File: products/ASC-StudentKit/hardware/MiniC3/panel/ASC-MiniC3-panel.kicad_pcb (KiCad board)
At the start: 2 copper layers, 96 x 100 mm, 128 parts, among them J1_1 PUMP, J1_2 PUMP, J1_3 PUMP, J1_4 PUMP, J1_5 CABLE, J1_6 CABLE, J1_7 CABLE, J1_8 CABLE, J3_1 AUX, J3_2 AUX, J3_3 AUX, J3_4 AUX, J4_1 FLOW (XH or 3.5 mm), J4_2 FLOW (XH or 3.5 mm), J4_3 FLOW (XH or 3.5 mm), J4_4 FLOW (XH or 3.5 mm), J5_1 I2C, J5_2 I2C, J5_3 I2C, J5_4 I2C, J6_1 RELAY 230V (MSTBVA), J6_2 RELAY 230V (MSTBVA), J6_3 RELAY 230V (MSTBVA), J6_4 RELAY 230V (MSTBVA), K1_1 HF46F/005-HS1, K1_2 HF46F/005-HS1, K1_3 HF46F/005-HS1, K1_4 HF46F/005-HS1, U1_1 ESP32-C3 Super Mini, U1_2 ESP32-C3 Super Mini, U1_3 ESP32-C3 Super Mini, U1_4 ESP32-C3 Super Mini, U1_5 AHT20, U1_6 AHT20, U1_7 AHT20, U1_8 AHT20, U2_1 DS1307Z+, U2_2 DS1307Z+, U2_3 DS1307Z+, U2_4 DS1307Z+, U3_1 ULN2003A, U3_2 ULN2003A, U3_3 ULN2003A, U3_4 ULN2003A, Y1_1 32.768k 12.5pF, Y1_2 32.768k 12.5pF, Y1_3 32.768k 12.5pF, Y1_4 32.768k 12.5pF

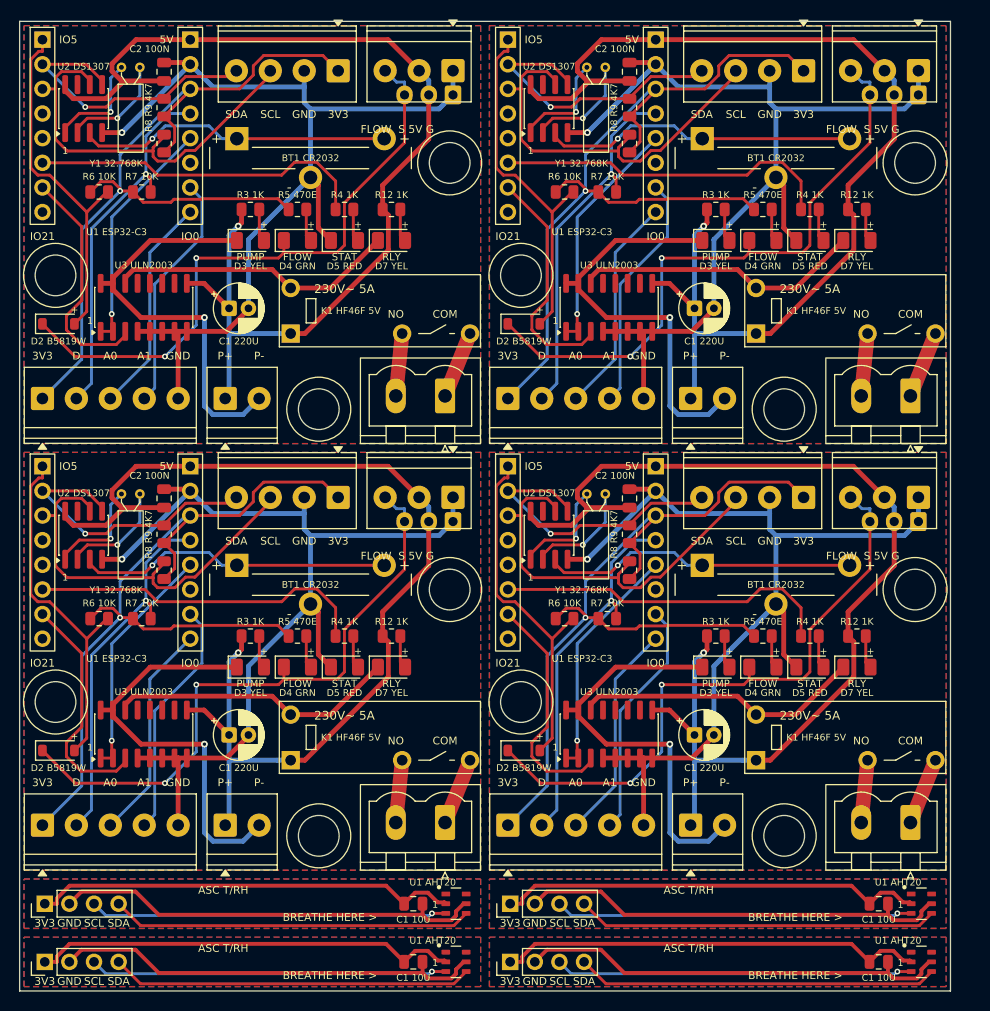
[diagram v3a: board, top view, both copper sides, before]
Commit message: ASC Mini-C3: slot-and-tab panel, flow pinout fix, BOM rates
- Panel now 98 x 98: 4 Minis + 2 AHT20 sticks, 2 mm routed slots with
  tabs and 0.5 mm mouse-bite holes (78, NPTH); no V-cut, as WhyPCB asked
  (JLC charges extra for V-cut). Zip carries a drawing and PANEL-README.
- Flow connector pinout fixed to the YF-S401 wiring: 1 = 5V (red),
  2 = GND (black, middle), 3 = SIG (yellow); silkscreen "FLOW S G 5V".
  Re-routed, DRC clean, mains clearance 5.00 mm.
- BOM: WhyPCB Rs 1,500 / 5 panels, Rs 2,000 / 10 panels (Rs 50 per Mini);
  kit about Rs 979; 2-kit sample about Rs 4,840 + LCSC shipping

Co-Authored-By: Claude Opus 5.5 <noreply@anthropic.com>
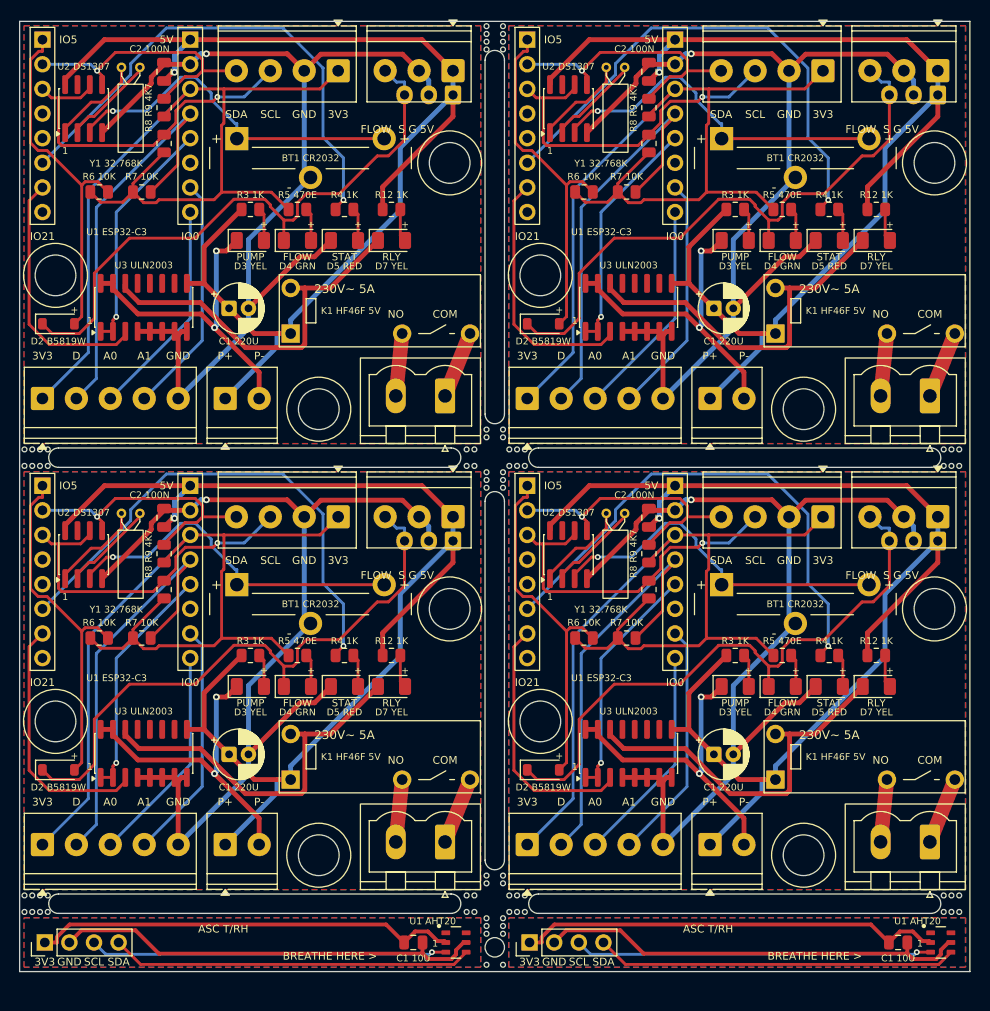
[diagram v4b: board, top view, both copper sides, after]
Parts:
- removed C1_7, C1_8: 10u, Capacitor_SMD:C_0805_2012Metric
- removed J1_7, J1_8: CABLE, Connector_PinHeader_2.54mm:PinHeader_1x04_P2.54mm_Vertical
- removed U1_7, U1_8: AHT20, ASC:Aosong_AHT20_DFN-6_3x3mm
- added MB1: , , F.Cu at (100.5, 104.2)
- added MB10: , , F.Cu at (148.2, 62.9)
- added MB11: , , F.Cu at (148.2, 102.1)
- added MB12: , , F.Cu at (148.2, 102.9)
- added MB13: , , F.Cu at (150.5, 104.2)
- added MB14: , , F.Cu at (151.3, 104.2)
- added MB15: , , F.Cu at (152.1, 104.2)
- added MB16: , , F.Cu at (195.3, 104.2)
- added MB17: , , F.Cu at (196.1, 104.2)
- added MB18: , , F.Cu at (196.9, 104.2)
- added MB19: , , F.Cu at (149.8, 60.5)
- added MB2: , , F.Cu at (101.3, 104.2)
- added MB20: , , F.Cu at (149.8, 61.3)
- added MB21: , , F.Cu at (149.8, 62.1)
- added MB22: , , F.Cu at (149.8, 62.9)
- added MB23: , , F.Cu at (149.8, 102.1)
- added MB24: , , F.Cu at (149.8, 102.9)
- added MB25: , , F.Cu at (100.5, 105.8)
- added MB26: , , F.Cu at (101.3, 105.8)
- added MB27: , , F.Cu at (102.1, 105.8)
- added MB28: , , F.Cu at (102.9, 105.8)
- added MB29: , , F.Cu at (146.1, 105.8)
- added MB3: , , F.Cu at (102.1, 104.2)
- added MB30: , , F.Cu at (146.9, 105.8)
- added MB31: , , F.Cu at (100.5, 150.2)
- added MB32: , , F.Cu at (101.3, 150.2)
- added MB33: , , F.Cu at (102.1, 150.2)
- added MB34: , , F.Cu at (102.9, 150.2)
- added MB35: , , F.Cu at (146.1, 150.2)
- added MB36: , , F.Cu at (146.9, 150.2)
- added MB37: , , F.Cu at (148.2, 106.5)
- added MB38: , , F.Cu at (148.2, 107.3)
- added MB39: , , F.Cu at (148.2, 108.1)
- added MB4: , , F.Cu at (102.9, 104.2)
- added MB40: , , F.Cu at (148.2, 148.1)
- added MB41: , , F.Cu at (148.2, 148.9)
- added MB42: , , F.Cu at (150.5, 105.8)
- added MB43: , , F.Cu at (151.3, 105.8)
- added MB44: , , F.Cu at (152.1, 105.8)
- added MB45: , , F.Cu at (195.3, 105.8)
- added MB46: , , F.Cu at (196.1, 105.8)
- added MB47: , , F.Cu at (196.9, 105.8)
- added MB48: , , F.Cu at (150.5, 150.2)
- added MB49: , , F.Cu at (151.3, 150.2)
- added MB5: , , F.Cu at (146.1, 104.2)
- added MB50: , , F.Cu at (152.1, 150.2)
- added MB51: , , F.Cu at (195.3, 150.2)
- added MB52: , , F.Cu at (196.1, 150.2)
- added MB53: , , F.Cu at (196.9, 150.2)
- added MB54: , , F.Cu at (149.8, 106.5)
- added MB55: , , F.Cu at (149.8, 107.3)
- added MB56: , , F.Cu at (149.8, 108.1)
- added MB57: , , F.Cu at (149.8, 148.1)
- added MB58: , , F.Cu at (149.8, 148.9)
- added MB59: , , F.Cu at (100.5, 151.8)
- added MB6: , , F.Cu at (146.9, 104.2)
- added MB60: , , F.Cu at (101.3, 151.8)
- added MB61: , , F.Cu at (102.1, 151.8)
- added MB62: , , F.Cu at (102.9, 151.8)
- added MB63: , , F.Cu at (146.1, 151.8)
- added MB64: , , F.Cu at (146.9, 151.8)
- added MB65: , , F.Cu at (148.2, 152.5)
- added MB66: , , F.Cu at (148.2, 153.3)
- added MB67: , , F.Cu at (148.2, 154.1)
- added MB68: , , F.Cu at (148.2, 157.3)
- added MB69: , , F.Cu at (150.5, 151.8)
- added MB7: , , F.Cu at (148.2, 60.5)
- added MB70: , , F.Cu at (151.3, 151.8)
- added MB71: , , F.Cu at (152.1, 151.8)
- added MB72: , , F.Cu at (195.3, 151.8)
- added MB73: , , F.Cu at (196.1, 151.8)
- added MB74: , , F.Cu at (196.9, 151.8)
- added MB75: , , F.Cu at (149.8, 152.5)
- added MB76: , , F.Cu at (149.8, 153.3)
- added MB77: , , F.Cu at (149.8, 154.1)
- added MB78: , , F.Cu at (149.8, 157.3)
- added MB8: , , F.Cu at (148.2, 61.3)
- added MB9: , , F.Cu at (148.2, 62.1)
- moved C1_6 4.47 mm to (190.6, 155.0)
- moved J1_6 4.47 mm to (152.6, 155.0)
- moved U1_6 4.47 mm to (195.0, 155.0)
- moved C1_5 4.00 mm to (140.6, 155.0)
- moved J1_5 4.00 mm to (102.6, 155.0)
- moved U1_5 4.00 mm to (145.0, 155.0)
- moved BT1_4 2.83 mm to (180.0, 118.1)
- moved C1_4 2.83 mm to (171.6, 135.6)
- moved C2_4 2.83 mm to (164.9, 111.2)
- moved D2_4 2.83 mm to (154.0, 137.2)
- moved D3_4 2.83 mm to (173.8, 128.6)
- moved D4_4 2.83 mm to (178.7, 128.6)
- moved D5_4 2.83 mm to (183.5, 128.6)
- moved D7_4 2.83 mm to (188.3, 128.6)
- moved H1_4 2.83 mm to (194.3, 120.6)
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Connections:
- J4_1 pad 1: B1/GND -> B1/+5V
- J4_1 pad 2: B1/+5V -> B1/GND
- J4_2 pad 1: B2/GND -> B2/+5V
- J4_2 pad 2: B2/+5V -> B2/GND
- J4_3 pad 1: B3/GND -> B3/+5V
- J4_3 pad 2: B3/+5V -> B3/GND
- J4_4 pad 1: B4/GND -> B4/+5V
- J4_4 pad 2: B4/+5V -> B4/GND
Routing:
- net B7/GND: track 44.8 -> 0.00 mm
- net B8/GND: track 44.8 -> 0.00 mm
- net B8/+3V3: track 44.2 -> 0.00 mm
- net B7/+3V3: track 44.2 -> 0.00 mm
- net B7/SDA: track 37.3 -> 0.00 mm
- net B8/SDA: track 37.3 -> 0.00 mm
- net B8/SCL: track 36.9 -> 0.00 mm, vias 1 -> 0
- net B7/SCL: track 36.9 -> 0.00 mm, vias 1 -> 0
- net B4/LED_STATUS: track 35.0 -> 52.9 mm, vias 0 -> 1
- net B2/LED_STATUS: track 35.0 -> 52.9 mm, vias 0 -> 1
- net B3/LED_STATUS: track 35.0 -> 52.9 mm, vias 0 -> 1
- net B1/LED_STATUS: track 35.0 -> 52.9 mm, vias 0 -> 1
- net B4/+5V: track 115.0 -> 130.3 mm
- net B3/+5V: track 115.0 -> 130.3 mm
- net B2/+5V: track 115.0 -> 130.3 mm
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- removed copper zone on B.Cu, net B7/GND
- removed copper zone on F.Cu, net B7/GND
- removed copper zone on B.Cu, net B8/GND
- removed copper zone on F.Cu, net B8/GND
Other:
- board size 96 x 100 mm -> 98 x 98 mm
- board text added: "ASC Mini-C3 panel 98 x 98: 4 x Mini-C3 + 2 x AHT20 stick. 2 mm routed slots (Edge.Cuts), tabs with 0.5 mm mouse-bite holes (NPTH drill). No V-cut."
- board text added: "FLOW S G 5V"
- board text removed: "ASC Mini-C3 panel 96 x 100: 4 x Mini-C3 + 4 x AHT20 stick. V-cut on all Cmts.User lines, 1/3 depth each side."
- board text removed: "FLOW S 5V G"
- board text removed: "V-CUT"

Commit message: ASC Mini-C3 panel: plain tabs (no mouse bites); 10 panels ordered
- Mouse-bite holes removed: WhyPCB says JLC may not accept them
  (MOUSE_BITES flag in tools/panel.py keeps the option). Plain tabs,
  narrowed to ~2 mm at the panel edges and ~5 mm at the slot crossings.
  Panel DRC: 0 errors.
- PANEL-README, README, BOM wording: routed slots, plain tabs, no V-cut,
  no mouse bites.
- Sourcing: 10 panels (40 Minis + 20 sticks) ordered from WhyPCB for
  Rs 2,000 on 2026-10-14.

Co-Authored-By: Claude Opus 5.5 <noreply@anthropic.com>
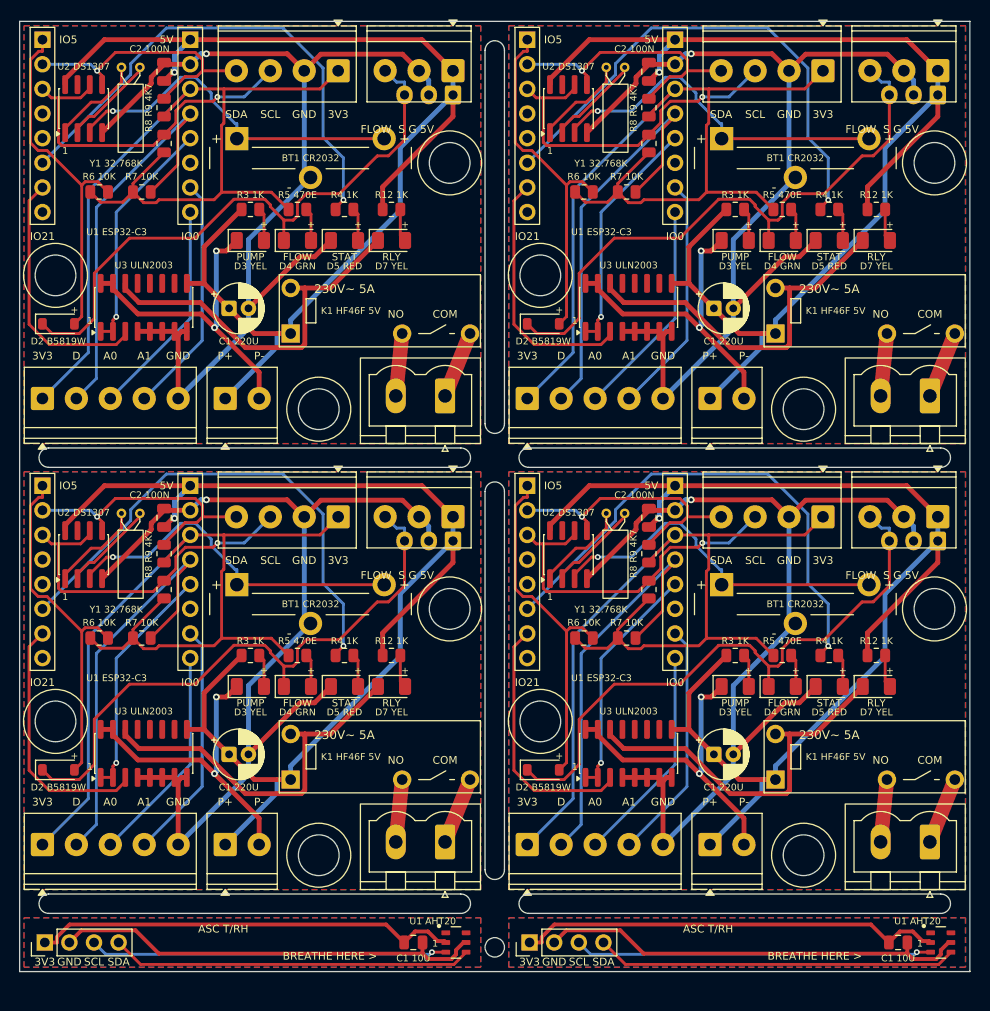
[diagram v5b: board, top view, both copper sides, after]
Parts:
- removed MB1, MB10, MB11, MB12, MB13, MB14, MB15, MB16, MB17, MB18, MB19, MB2, MB20, MB21, MB22, MB23, MB24, MB25, MB26, MB27, MB28, MB29, MB3, MB30, MB31, MB32, MB33, MB34, MB35, MB36, MB37, MB38, MB39, MB4, MB40, MB41, MB42, MB43, MB44, MB45, MB46, MB47, MB48, MB49, MB5, MB50, MB51, MB52, MB53, MB54, MB55, MB56, MB57, MB58, MB59, MB6, MB60, MB61, MB62, MB63, MB64, MB65, MB66, MB67, MB68, MB69, MB7, MB70, MB71, MB72, MB73, MB74, MB75, MB76, MB77, MB78, MB8, MB9: , 
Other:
- outline, holes or cut-outs redrawn
- board text added: "ASC Mini-C3 panel 98 x 98: 4 x Mini-C3 + 2 x AHT20 stick. 2 mm routed slots (Edge.Cuts), plain break-away tabs (no mouse bites). No V-cut."
- board text removed: "ASC Mini-C3 panel 98 x 98: 4 x Mini-C3 + 2 x AHT20 stick. 2 mm routed slots (Edge.Cuts), tabs with 0.5 mm mouse-bite holes (NPTH drill). No V-cut."
